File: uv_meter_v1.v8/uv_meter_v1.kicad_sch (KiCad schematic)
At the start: 47 parts, among them J101 CONN_DC_PWR_JACK, J401 SD, J501 VH, SW101 SK-12F17-G, SW601 BUTTON_PTS64, U101 3.3V, 200mA, U102 3.3V, 200mA, U103 5V, 200mA, U201 Socket STM32, U301 LMV358, U501 MCP2562

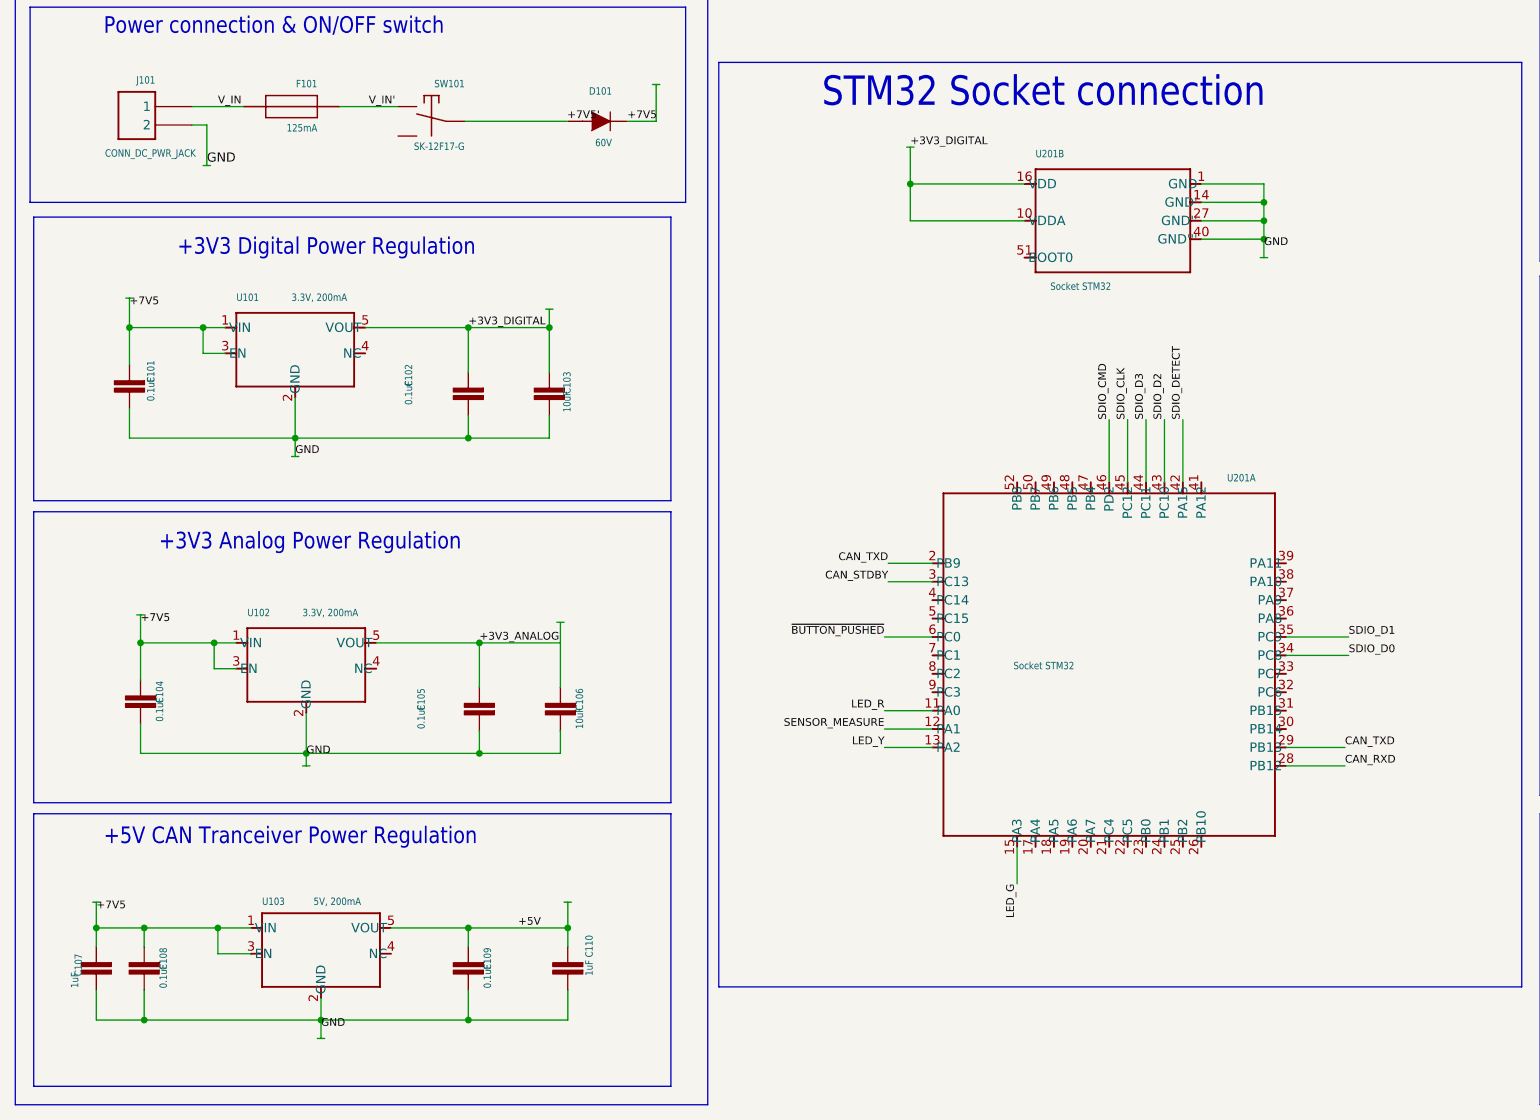
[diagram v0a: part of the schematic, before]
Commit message: Update schematic from library
Since some symbols have been updated to look better and for later and easier
updates a schematic update from library was required.

NOTE :
  The current goal is to fix all symbols and schematic but it should look like
  what the original project was. No symbol redesign is to be performed at this
  stage : we will tag this as the V0 since the PCB has been assembled in the
  past and debugged. Debugged version wil be V1 since it is functionnal ;
  additionnal documentation will be committed as well to explain bug fixes.
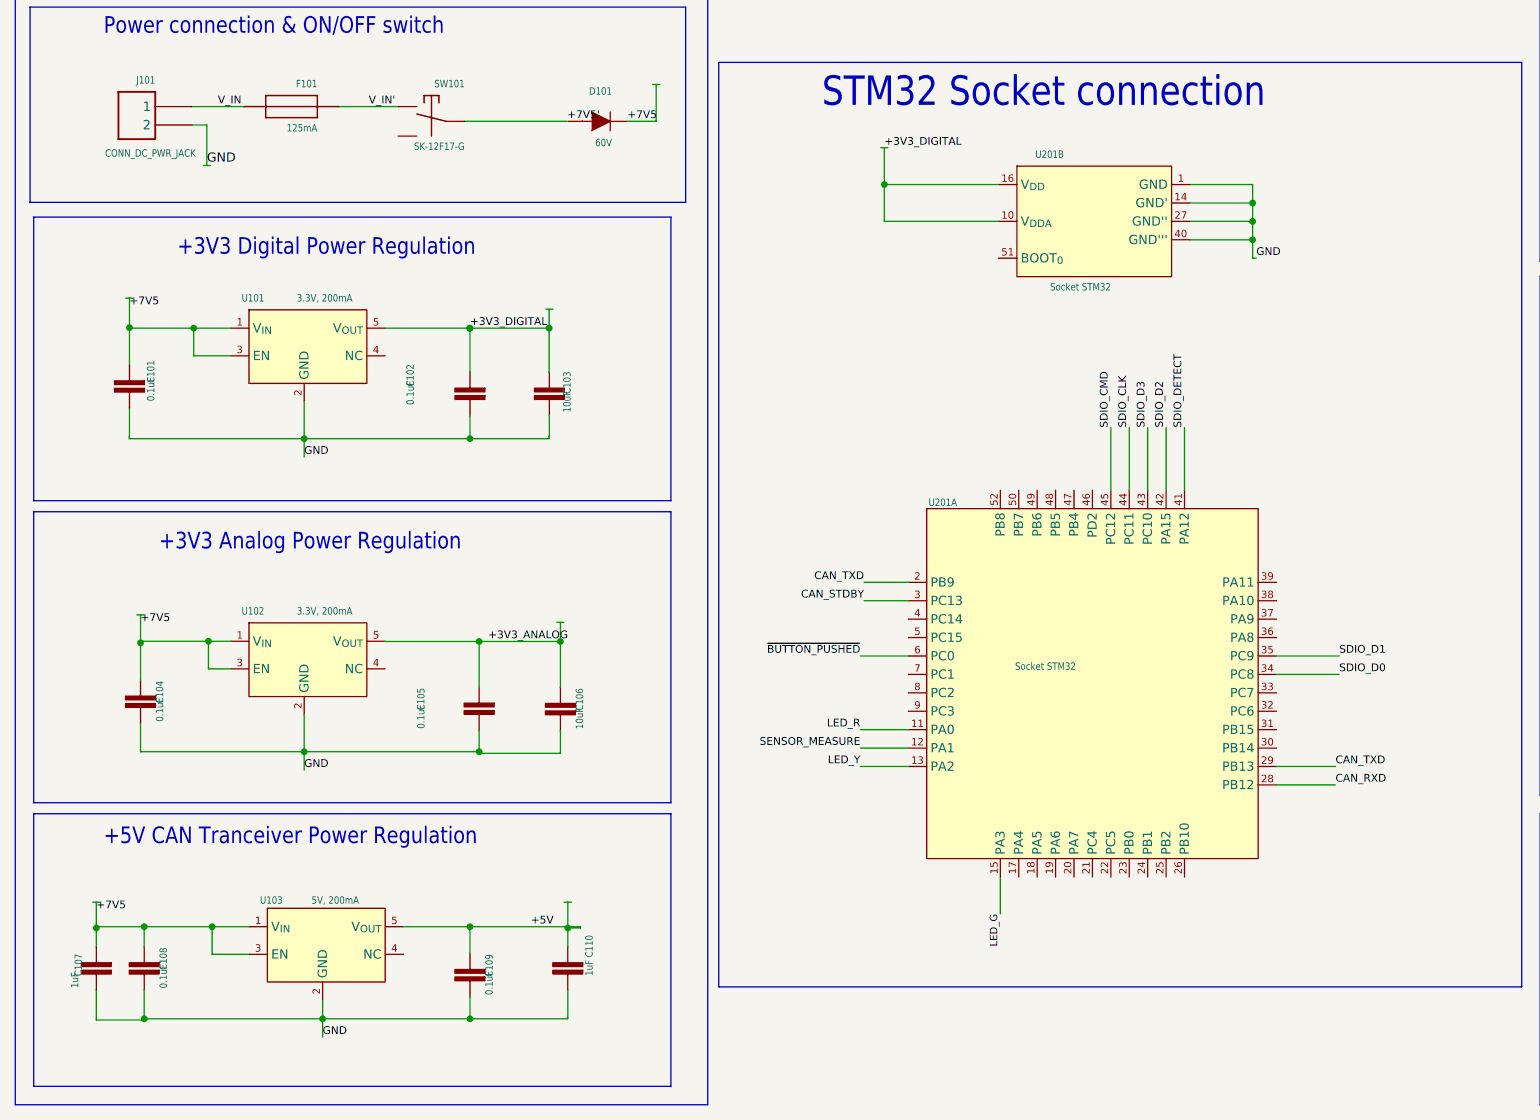
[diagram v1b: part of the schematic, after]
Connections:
- net SDIO_CLK: now also U201.44 (PC11); no longer U201.45 (PC12)
- net SDIO_CMD: now also U201.45 (PC12); no longer U201.46 (PD2)
- net SDIO_D2: now also U201.42 (PA15); no longer U201.43 (PC10)
- net SDIO_D3: now also U201.43 (PC10); no longer U201.44 (PC11)
- net SDIO_DETECT: now also U201.41 (PA12); no longer U201.42 (PA15)
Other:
- moved on the sheet: C109

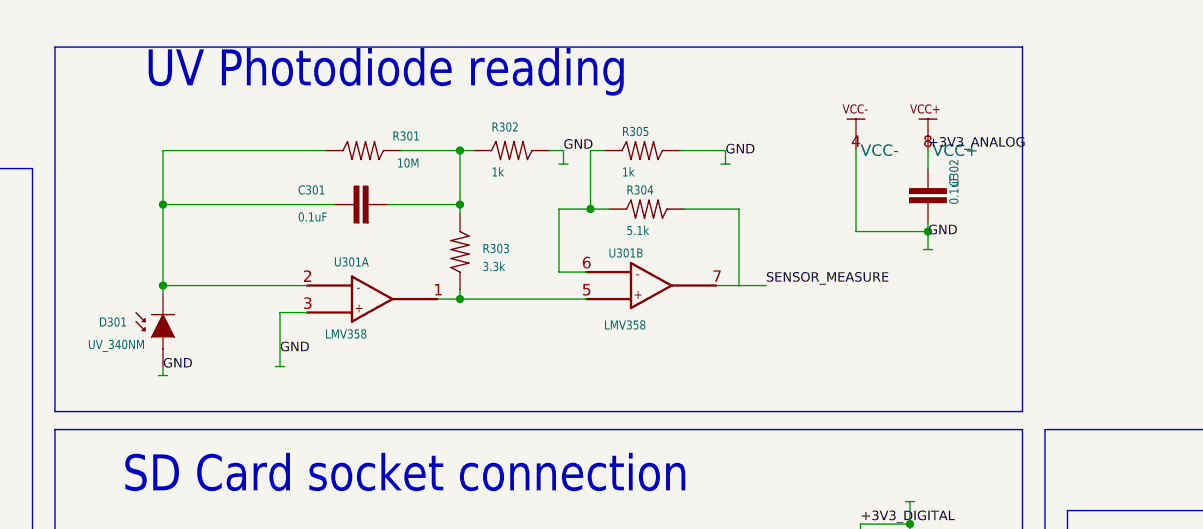
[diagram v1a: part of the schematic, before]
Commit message: Update LMV358 symbol
* Update LMV358 symbol in local library : use shapes that allow to fill
  symbol and break power supply sub-symbol into 2 different entities
  for ease of use reasons.
* Update design schematic accordingly.
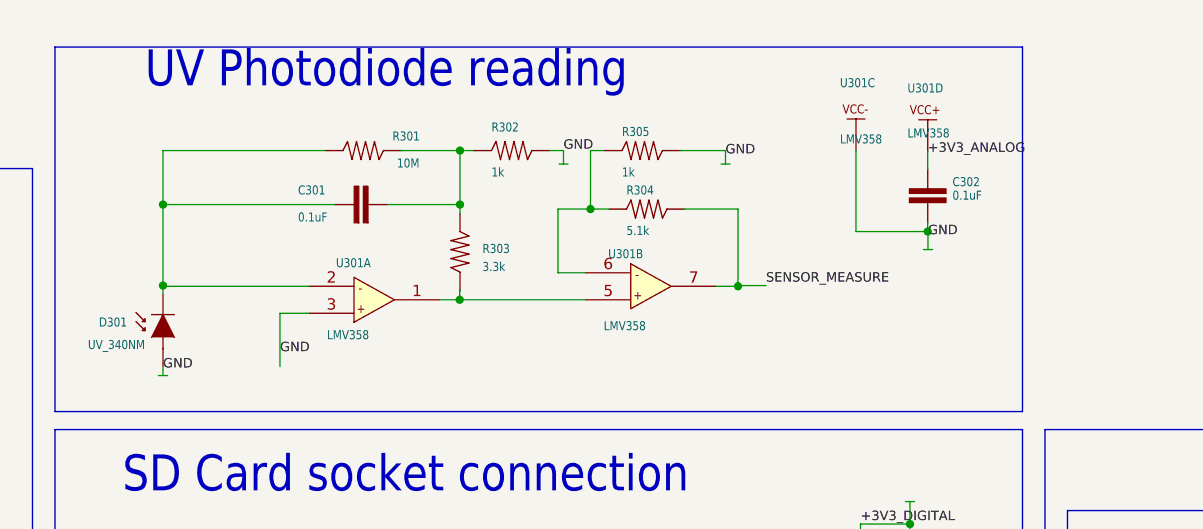
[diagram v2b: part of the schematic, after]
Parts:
- added unit 4 of U301
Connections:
- net +3V3_ANALOG: now also U301.8 (VCC+); no longer U301.8 (VCC+)

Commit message: Update Power symbols in schematic
* Remove old power "symbols" created with labels and make use of KiCad's
  power symbols from standard library instead
* Place unconnected marks where required. This will comply with KiCad's
  standards if any ERC check is performed
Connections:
- net +5V: now also C502.1 (2), U501.3 (VDD)
- net GND: now also C501.2 (1), C502.2 (1)
- net +3V3_ANALOG renamed +3.3VADC
- net +3V3_DIGITAL renamed +3.3V
- net +7V5 renamed +7.5V
- net +7V5' renamed +7V5_{IN}
- net V_IN renamed V_{IN}
- net V_IN' renamed V_{IN}^{fused}
- no-connect marks 0 -> 34
